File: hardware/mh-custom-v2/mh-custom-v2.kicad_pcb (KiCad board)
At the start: 2 copper layers, 95.7 x 99.3 mm, 107 parts, among them J1 Conn_01x03_Male, J3 Conn_02x19_Top_Bottom, J4 Conn_02x19_Top_Bottom, J5 Screw_Terminal_01x04, J6 Screw_Terminal_01x04, J7 Screw_Terminal_01x04, J8 Screw_Terminal_01x04, SW1 SW_DIP_x04, T1 AO3400A, T2 AO3400A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

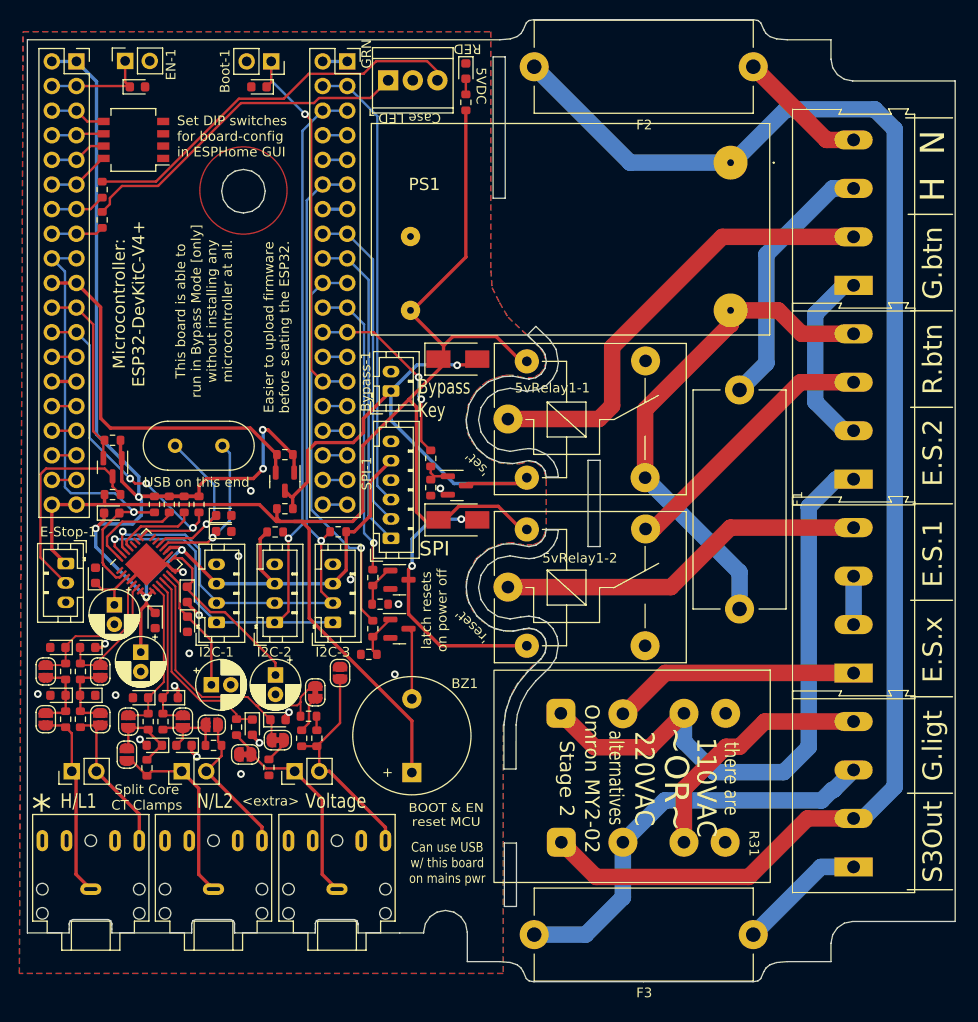
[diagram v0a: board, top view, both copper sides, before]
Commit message: improved some of the connections for easier soldering/production
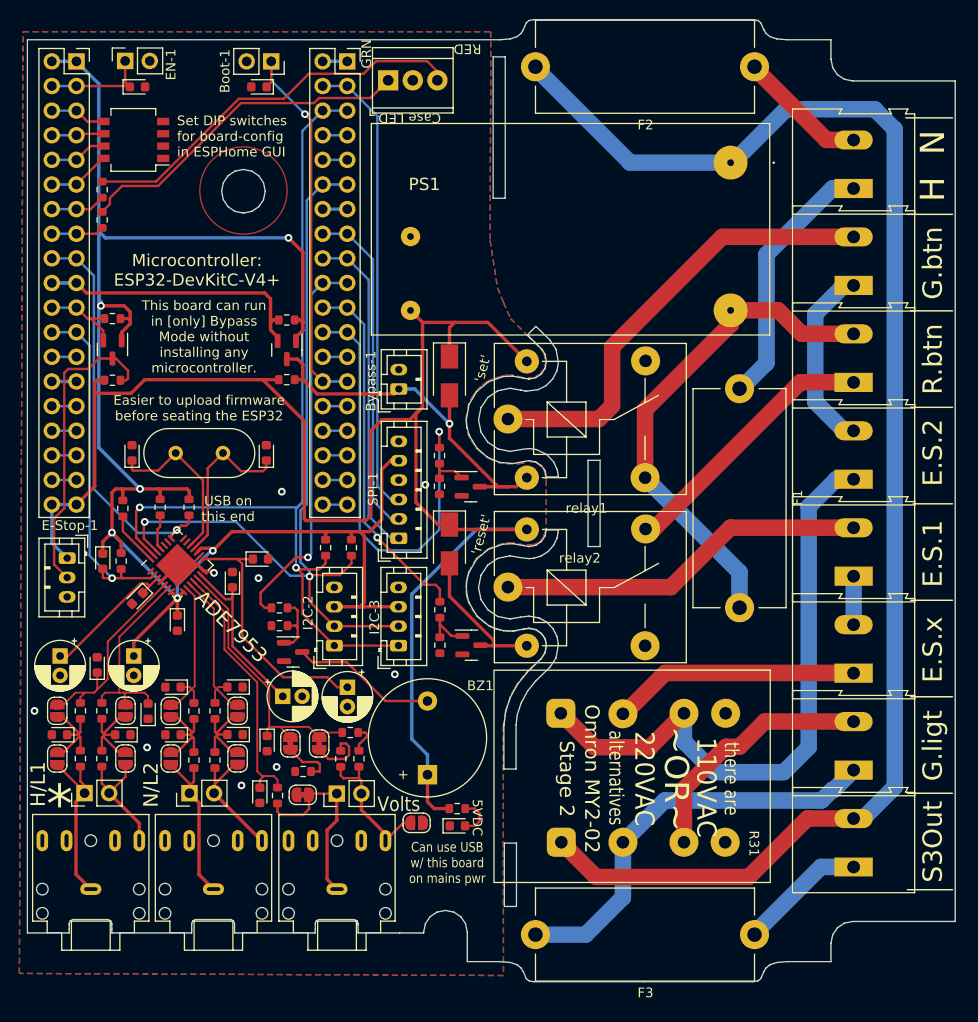
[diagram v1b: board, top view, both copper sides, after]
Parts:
- removed I2C-1: Conn_01x04_Female, Connector_JST:JST_PH_B4B-PH-K_1x04_P2.00mm_Vertical
- added J10: Screw_Terminal_01x02, TerminalBlock:TerminalBlock_Altech_AK300-2_P5.00mm, F.Cu at (118.2, 85.7)
- added J11: Screw_Terminal_01x02, TerminalBlock:TerminalBlock_Altech_AK300-2_P5.00mm, F.Cu at (118.2, 95.7)
- added J12: Screw_Terminal_01x02, TerminalBlock:TerminalBlock_Altech_AK300-2_P5.00mm, F.Cu at (118.2, 105.7)
- added J9: Screw_Terminal_01x02, TerminalBlock:TerminalBlock_Altech_AK300-2_P5.00mm, F.Cu at (118.2, 75.7)
- J5, J6, J7, J8: value Screw_Terminal_01x04 -> Screw_Terminal_01x02; footprint TerminalBlock:TerminalBlock_Altech_AK300-4_P5.00mm -> TerminalBlock:TerminalBlock_Altech_AK300-2_P5.00mm
- relay1: renamed from 5vRelay1-1; value SANYOU_SRD_Form_C -> JQC-3FF/005-1ZS(551)
- relay2: renamed from 5vRelay1-2; value SANYOU_SRD_Form_C -> JQC-3FF/005-1ZS(551)
- moved D2 77.9 mm to (77.3, 104.0), turned to 0 degrees
- moved R26 72.9 mm to (77.3, 102.2), turned to 180 degrees
- moved J8 42.5 mm to (118.2, 65.7)
- moved J7 32.5 mm to (118.2, 55.7)
- moved J3 22.9 mm to (36.7, 48.0)
- moved J4 22.9 mm to (64.7, 48.0)
- moved J6 22.5 mm to (118.2, 45.7)
- moved JP1 17.4 mm to (73.1, 103.7), turned to 180 degrees
- moved R32 13.9 mm to (59.7, 51.8)
- moved T5 13.6 mm to (59.7, 54.9)
- moved R33 13.3 mm to (59.7, 58.0)
- moved R3 12.6 mm to (41.7, 51.7)
- moved J5 12.5 mm to (118.2, 35.7)
- moved T2 12.2 mm to (41.7, 54.8)
- moved R4 11.8 mm to (41.7, 58.0)
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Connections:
- J3 pad 17: ade7953-reset -> ade7953-IRQ
- J3 pad 18: ade7953-reset -> ade7953-IRQ
- J3 pad 23: ade7953-IRQ -> ade7953-reset
- J3 pad 24: ade7953-IRQ -> ade7953-reset
- J5 pad 1: Member-E-Stop-sw2-1 -> H/L1
- J5 pad 2: Member-Green-Button-1 -> N/L2
- J6 pad 1: Member-E-Stop-sw2-2 -> Member-E-Stop-sw2-1
- J6 pad 2: Member-E-Stop-sw2-1 -> Member-Green-Button-1
- J7 pad 1: Member-E-Stop-aux-2 -> Member-Red-Reset-Button-2
- J7 pad 2: Member-E-Stop-aux-1 -> Member-Red-Reset-Button-1
- J8 pad 1: S3-Contactor-Control -> Member-E-Stop-sw2-2
- J8 pad 2: mains-fused-N/L2 -> Member-E-Stop-sw2-1
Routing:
- net set3v: track 19.9 -> 45.3 mm, vias 2 -> 1
- net +3V3: track 162.8 -> 183.4 mm
- net read-bypass: track 57.2 -> 39.5 mm
- net /mainslevelcontrol/stage1relays/dcp2: track 29.1 -> 15.2 mm, vias 2 -> 0
- net +5V: track 158.4 -> 169.3 mm
- net read-E-Stop: track 19.5 -> 8.66 mm
- net ade7953-reset: track 47.5 -> 36.8 mm
- net 3vRead-Bypass: track 39.2 -> 28.8 mm
- net Net-(C16-Pad1): track 5.60 -> 14.6 mm
- net Net-(E-Stop-1-Pad2): track 22.5 -> 31.5 mm
- net GND: track 25.7 -> 16.9 mm, vias 18 -> 9
- net Net-(C17-Pad1): track 18.3 -> 26.2 mm
- net SDA: track 78.0 -> 85.9 mm
- net VP_IN: track 22.7 -> 15.0 mm
- net /microcontroller/lightsounds/dcp1: track 7.38 -> 15.0 mm
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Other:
- board text added: "ADE7953"
- board text added: "Easier to upload firmware before seating the ESP32"
- board text added: "This board can run in [only] Bypass Mode without installing any microcontroller."
- board text added: "Volts"
- board text removed: "<extra>"
- board text removed: "BOOT & EN reset MCU"
- board text removed: "Bypass Key"
- board text removed: "Easier to upload firmware before seating the ESP32."
- board text removed: "SPI"
- board text removed: "Split Core CT Clamps"
- board text removed: "This board is able to run in Bypass Mode [only] without installing any microcontroller at all."
- board text removed: "Voltage"
- board text removed: "latch resets on power off"

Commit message: laptop back, coordinating efforts
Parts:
- moved F2 0.09 mm to (96.4, 25.6)
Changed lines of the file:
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@@
   )
   (footprint "Fuse:Fuseholder_Cylinder-5x20mm_Stelvio-Kontek_PTF78_Horizontal_Open" (layer "F.Cu")
-    (at 96.525 25.675 180)
+    (at 96.435 25.65 180)
     (descr "https://www.tme.eu/en/Document/3b48dbe2b9714a62652c97b08fcd464b/PTF78.pdf")
     (tags "Fuseholder horizontal open 5x20 Stelvio-Kontek PTF/78")
@@
   )
   (footprint "CFM06S050-E - Cincon:CFM06S050E" (layer "F.Cu")
-    (at 105.485 35.57 180)
+    (at 105.455 35.59 180)
     (descr "CFM06S050-E-2")
     (tags "Power Supply")
@@
     (property "Sheetname" "stage1relays")
     (attr through_hole)
-    (fp_text reference "PS1" (at 31.588 -2.238) (layer "F.SilkS")
+    (fp_text reference "PS1" (at 16.51 -6.87 180) (layer "F.SilkS")
       (effects (font (size 1.27 1.27) (thickness 0.254)))
     )
-    (fp_text value "CFM06S050" (at 16.51 -6.87) (layer "F.SilkS") hide
+    (fp_text value "CFM06S050" (at 16.51 -6.87 180) (layer "F.SilkS") hide
       (effects (font (size 1.27 1.27) (thickness 0.254)))
     )
-    (fp_text user "${REFERENCE}" (at 16.51 -6.87) (layer "F.Fab")
+    (fp_text user "${REFERENCE}" (at 16.51 -6.87 180) (layer "F.Fab")
       (effects (font (size 1.27 1.27) (thickness 0.254)))
     )
-    (fp_line (start -4.5 0) (end -4.5 0) (layer "F.SilkS") (width 0.1))
-    (fp_line (start 37.06 4.04) (end 37.06 -17.78) (layer "F.SilkS") (width 0.1))
-    (fp_line (start -4.04 4.04) (end 37.06 4.04) (layer "F.SilkS") (width 0.1))
     (fp_line (start -4.4 0) (end -4.4 0) (layer "F.SilkS") (width 0.1))
-    (fp_line (start 37.06 -17.78) (end -4.04 -17.78) (layer "F.SilkS") (width 0.1))
     (fp_line (start -4.04 -17.78) (end -4.04 4.04) (layer "F.SilkS") (width 0.1))
+    (fp_line (start -4.04 4.04) (end 37.06 4.04) (layer "F.SilkS") (width 0.1))
+    (fp_line (start 37.06 -17.78) (end -4.04 -17.78) (layer "F.SilkS") (width 0.1))
+    (fp_line (start 37.06 4.04) (end 37.06 -17.78) (layer "F.SilkS") (width 0.1))
+    (fp_line (start -4.5 0) (end -4.5 0) (layer "F.SilkS") (width 0.1))
     (fp_arc (start -4.5 0) (mid -4.45 -0.05) (end -4.4 0) (layer "F.SilkS") (width 0.1))
     (fp_arc (start -4.4 0) (mid -4.45 0.05) (end -4.5 0) (layer "F.SilkS") (width 0.1))
-    (fp_line (start -4.64 4.64) (end 37.66 4.64) (layer "F.CrtYd") (width 0.1))
-    (fp_line (start -4.64 -18.38) (end -4.64 4.64) (layer "F.CrtYd") (width 0.1))
     (fp_line (start 37.66 4.64) (end 37.66 -18.38) (layer "F.CrtYd") (width 0.1))
     (fp_line (start 37.66 -18.38) (end -4.64 -18.38) (layer "F.CrtYd") (width 0.1))
-    (fp_line (start 37.06 -17.78) (end -4.04 -17.78) (layer "F.Fab") (width 0.2))
+    (fp_line (start -4.64 -18.38) (end -4.64 4.64) (layer "F.CrtYd") (width 0.1))
+    (fp_line (start -4.64 4.64) (end 37.66 4.64) (layer "F.CrtYd") (width 0.1))
     (fp_line (start -4.04 -17.78) (end -4.04 4.04) (layer "F.Fab") (width 0.2))
     (fp_line (start -4.04 4.04) (end 37.06 4.04) (layer "F.Fab") (width 0.2))
+    (fp_line (start 37.06 -17.78) (end -4.04 -17.78) (layer "F.Fab") (width 0.2))
     (fp_line (start 37.06 4.04) (end 37.06 -17.78) (layer "F.Fab") (width 0.2))
     (pad "1" thru_hole circle (at 0 0 180) (size 3.5 3.5) (drill 0.7) (layers *.Cu *.Mask)
@@
   (segment (start 61.505 62.23) (end 57.235 57.96) (width 0.35) (layer "F.Cu") (net 4))
   (segment (start 76.485 52.58) (end 76.485 55.57) (width 0.35) (layer "F.Cu") (net 4))
+  (segment (start 73.655 52.05) (end 73.705 52.05) (width 0.35) (layer "F.Cu") (net 4))
   (segment (start 39.895 59.37) (end 39.895 58.23) (width 0.35) (layer "F.Cu") (net 4))
   (segment (start 73.025 70.62) (end 73.025 61.46) (width 0.35) (layer "F.Cu") (net 4))
@@
   (segment (start 73.025 61.46) (end 73.315 61.17) (width 0.35) (layer "F.Cu") (net 4))
   (segment (start 39.895 59.37) (end 39.895 68.95) (width 0.35) (layer "F.Cu") (net 4))
+  (segment (start 72.465 50.81) (end 72.465 50.86) (width 0.35) (layer "F.Cu") (net 4))
   (segment (start 84.465 56.07) (end 80.445 52.05) (width 0.35) (layer "F.Cu") (net 4))
   (segment (start 61.69 72.495) (end 61.505 72.31) (width 0.35) (layer "F.Cu") (net 4))
@@
   (segment (start 73.705 52.05) (end 77.015 52.05) (width 0.35) (layer "F.Cu") (net 4))
   (segment (start 39.895 58.23) (end 40.105 58.02) (width 0.35) (layer "F.Cu") (net 4))
+  (segment (start 72.465 50.86) (end 73.655 52.05) (width 0.35) (layer "F.Cu") (net 4))
   (segment (start 73.315 61.17) (end 72.405 62.08) (width 0.35) (layer "F.Cu") (net 4))
   (segment (start 72.405 62.08) (end 69.515 62.08) (width 0.35) (layer "F.Cu") (net 4))
@@
   (segment (start 67.85 72.495) (end 61.69 72.495) (width 0.35) (layer "F.Cu") (net 4))
   (segment (start 45.045 57.96) (end 43.635 59.37) (width 0.35) (layer "F.Cu") (net 4))
-  (segment (start 72.465 50.81) (end 73.705 52.05) (width 0.35) (layer "F.Cu") (net 4))
   (segment (start 73.705 60.78) (end 73.315 61.17) (width 0.35) (layer "F.Cu") (net 4))
   (segment (start 77.015 52.05) (end 76.485 52.58) (width 0.35) (layer "F.Cu") (net 4))
@@
   (segment (start 109.185 45.04) (end 116 38.225) (width 1.7) (layer "B.Cu") (net 32))
   (segment (start 116 38.225) (end 118.175 38.225) (width 1.7) (layer "B.Cu") (net 32))
-  (segment (start 115.375 33.225) (end 107.825 25.675) (width 1.7) (layer "F.Cu") (net 33))
+  (segment (start 115.375 33.225) (end 107.865 25.715) (width 1.7) (layer "F.Cu") (net 33))
+  (segment (start 107.865 25.715) (end 107.865 25.65) (width 1.7) (layer "F.Cu") (net 33))
   (segment (start 118.175 33.225) (end 115.375 33.225) (width 1.7) (layer "F.Cu") (net 33))
   (segment (start 91.605 109.26) (end 107.375 109.26) (width 1.7) (layer "F.Cu") (net 34))
@@
   (segment (start 88.025 105.68) (end 91.605 109.26) (width 1.7) (layer "F.Cu") (net 34))
   (segment (start 113.41 103.225) (end 118.175 103.225) (width 1.7) (layer "F.Cu") (net 34))
-  (segment (start 120.365 30.07) (end 111.195 30.07) (width 1.7) (layer "B.Cu") (net 34))
-  (segment (start 105.485 35.57) (end 95.12 35.57) (width 1.7) (layer "B.Cu") (net 34))
-  (segment (start 122.415 99.975) (end 122.415 32.12) (width 1.7) (layer "B.Cu") (net 34))
-  (segment (start 95.12 35.57) (end 85.225 25.675) (width 1.7) (layer "B.Cu") (net 34))
-  (segment (start 119.165 103.225) (end 122.415 99.975) (width 1.7) (layer "B.Cu") (net 34))
-  (segment (start 111.195 30.07) (end 105.51 35.755) (width 1.7) (layer "B.Cu") (net 34))
+  (segment (start 105.675 35.59) (end 105.455 35.59) (width 1.7) (layer "B.Cu") (net 34))
   (segment (start 118.175 103.225) (end 119.165 103.225) (width 1.7) (layer "B.Cu") (net 34))
   (segment (start 122.415 32.12) (end 120.365 30.07) (width 1.7) (layer "B.Cu") (net 34))
+  (segment (start 105.485 35.57) (end 95.12 35.57) (width 1.7) (layer "B.Cu") (net 34))
+  (segment (start 95.12 35.57) (end 85.265 25.715) (width 1.7) (layer "B.Cu") (net 34))
+  (segment (start 85.265 25.715) (end 85.265 25.65) (width 1.7) (layer "B.Cu") (net 34))
+  (segment (start 119.165 103.225) (end 122.415 99.975) (width 1.7) (layer "B.Cu") (net 34))
+  (segment (start 122.415 99.975) (end 122.415 32.12) (width 1.7) (layer "B.Cu") (net 34))
+  (segment (start 111.195 30.07) (end 105.675 35.59) (width 1.7) (layer "B.Cu") (net 34))
+  (segment (start 120.365 30.07) (end 111.195 30.07) (width 1.7) (layer "B.Cu") (net 34))
   (segment (start 114.81 108.225) (end 107.825 115.21) (width 1.7) (layer "B.Cu") (net 35))
   (segment (start 118.175 108.225) (end 114.81 108.225) (width 1.7) (layer "B.Cu") (net 35))

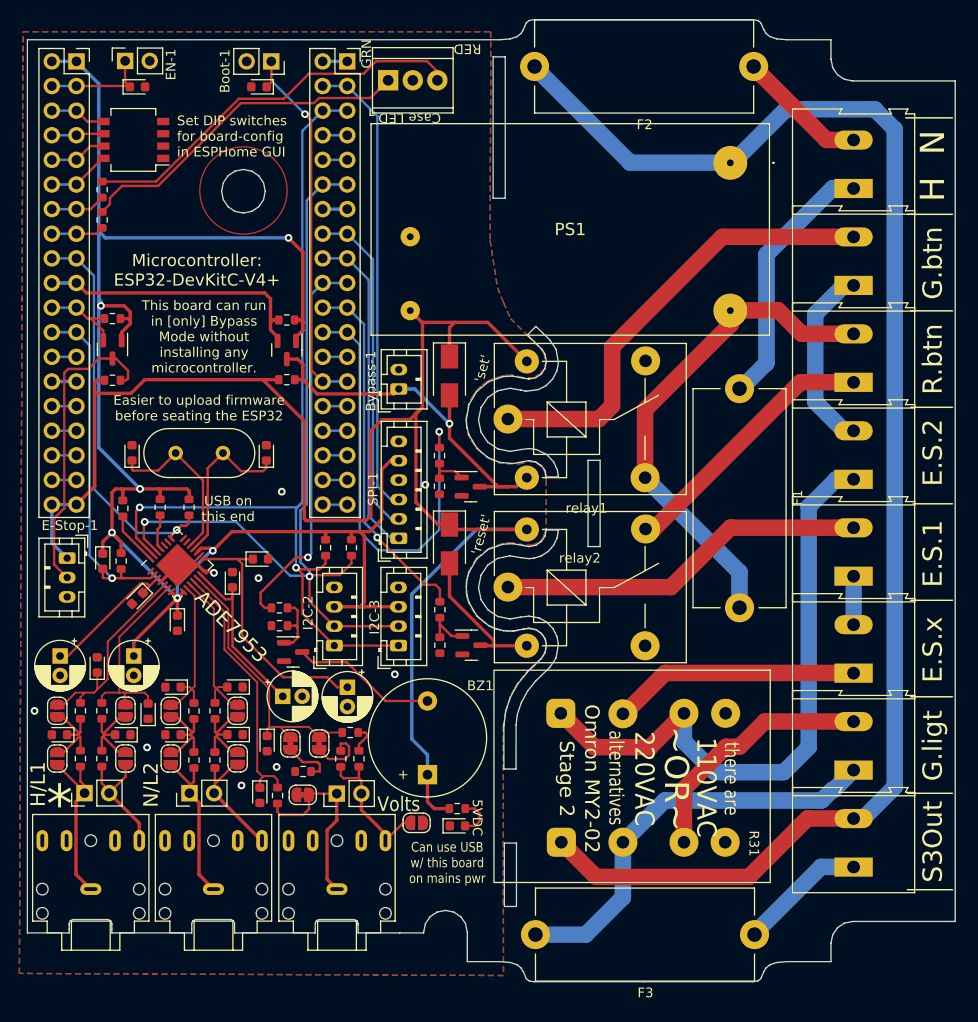
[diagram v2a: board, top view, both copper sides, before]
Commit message: added linear regulator for 3.3V peripherals and ADE7953 reset jumper
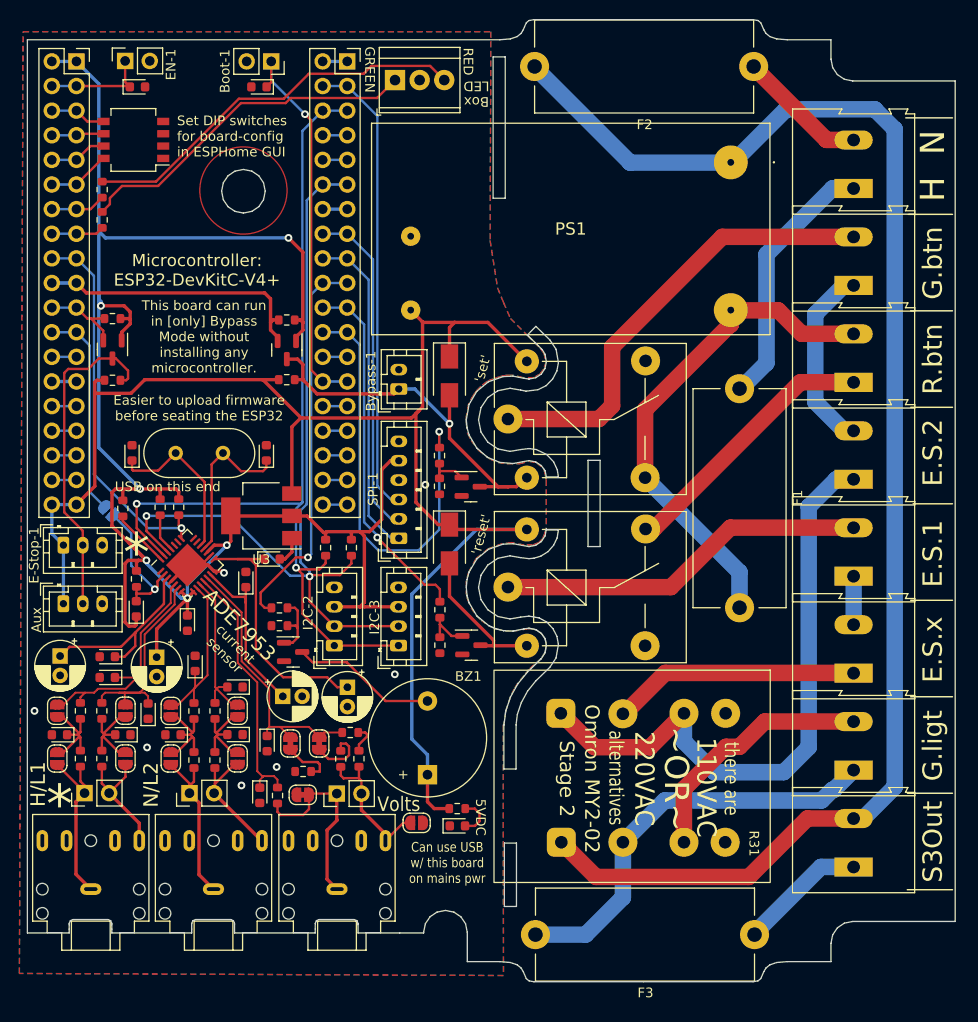
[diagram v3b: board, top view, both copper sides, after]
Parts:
- added E-Stop-2: Conn_01x03_Female, Connector_JST:JST_PH_B3B-PH-K_1x03_P2.00mm_Vertical, F.Cu at (36.7, 81.1)
- added JP13: software-reset, Jumper:SolderJumper-2_P1.3mm_Open_RoundedPad1.0x1.5mm, B.Cu at (41.4, 71.5)
- added U3: AMS1117-3.3, Package_TO_SOT_SMD:SOT-223-3_TabPin2, F.Cu at (57.1, 72.0)
- moved C16 6.76 mm to (41.2, 86.5), turned to 180 degrees
- moved C15 6.01 mm to (44.2, 81.6), turned to 90 degrees
- moved C9 3.34 mm to (50.2, 87.2), turned to 90 degrees
- moved R22 2.43 mm to (44.2, 78.5)
- moved C14 2.36 mm to (46.3, 87.6)
- moved C7 1.66 mm to (41.2, 88.7), turned to 180 degrees
- moved E-Stop-1 1.40 mm to (36.7, 75.0), turned to 0 degrees
- moved C22 1.38 mm to (55.5, 78.6)
- moved C17 1.20 mm to (58.2, 76.5)
- moved R23 1.06 mm to (48.6, 71.1)
- moved C13 1.04 mm to (49.4, 83.1)
- moved U2 1.04 mm to (49.4, 77.1)
- moved J1 0.71 mm to (73.4, 27.1)
- moved PS1 0.07 mm to (105.5, 35.5)
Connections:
- C15 pad 2: ade7953-reset -> Net-(C15-Pad2)
- R22 pad 1: ade7953-reset -> Net-(C15-Pad2)
- U2 pad 2: ade7953-reset -> Net-(C15-Pad2)
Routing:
- net ade7953-reset: track 36.8 -> 21.7 mm, vias 1 -> 0
- net Net-(C15-Pad2): track 0.00 -> 14.8 mm, vias 0 -> 1
- net +3V3: track 183.4 -> 194.4 mm
- net +5V: track 169.3 -> 162.2 mm
- net Net-(C16-Pad1): track 14.6 -> 19.7 mm
- net GND: track 16.9 -> 19.9 mm, vias 9 -> 7
- net IAP: track 21.4 -> 24.1 mm
- net Net-(E-Stop-1-Pad2): track 31.5 -> 34.0 mm
- net ade7953-IRQ: track 41.1 -> 39.4 mm
- net IAN: track 20.9 -> 22.5 mm
- net IBP: track 16.4 -> 18.0 mm
- net SDA: track 85.9 -> 86.8 mm
- net Net-(C17-Pad1): track 26.2 -> 27.2 mm
- net SCL: track 94.2 -> 95.0 mm
- net Net-(J1-Pad1): track 35.5 -> 36.2 mm
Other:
- board text added: "ADE7953 reset pin connect"
- board text added: "Aux"
- board text added: "Box LED"
- board text added: "GREEN"
- board text added: "current sensor"
- board text removed: "Case LED"
- board text removed: "GRN"
